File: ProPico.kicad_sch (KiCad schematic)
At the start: 16 parts

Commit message: started layout
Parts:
- removed U?: RP2040, QFN40P700X700X90-57N, symbol RP2040:RP2040
- removed U?: AMS1117-3.3, Package_TO_SOT_SMD:SOT-223-3_TabPin2, symbol Regulator_Linear:AMS1117-3.3
- added C1, C2: 18p, Capacitor_SMD:C_0402_1005Metric, symbol Device:C
- added C10, C12, C13, C14, C15, C16, C17, C7, C8: 100n, Capacitor_SMD:C_0402_1005Metric, symbol Device:C
- added C11, C9: 1u, Capacitor_SMD:C_0402_1005Metric, symbol Device:C
- added C2: 100n, Capacitor_SMD:C_0402_1005Metric_Pad0.74x0.62mm_HandSolder, symbol Device:C
- added C9: 10n C0G, Capacitor_SMD:C_0603_1608Metric_Pad1.08x0.95mm_HandSolder, symbol Device:C
- added D2, D3: LED, LED_SMD:LED_0603_1608Metric_Pad1.05x0.95mm_HandSolder, symbol Device:LED
- added J2: SWD, connector:Pico_4pin, symbol Connector_Generic:Conn_01x04
- added J3: LEFT, connector:Pico_20pin, symbol Connector_Generic:Conn_01x20
- added J4: RIGHT, connector:Pico_20pin, symbol Connector_Generic:Conn_01x20
- added JP1: EEPROM_WP, Jumper:SolderJumper-3_P2.0mm_Open_TrianglePad1.0x1.5mm, symbol Jumper:SolderJumper_3_Open
- added JP2: VREF, Jumper:SolderJumper-2_P1.3mm_Open_TrianglePad1.0x1.5mm, symbol Jumper:Jumper_2_Bridged
- added R3 (x3): 1k, Resistor_SMD:R_0402_1005Metric, symbol Device:R
- added R3 (x2): 4.7k, Resistor_SMD:R_0402_1005Metric, symbol Device:R
- added R4, R5: 27, Resistor_SMD:R_0402_1005Metric, symbol Device:R
- added R6: 5R, Resistor_SMD:R_0805_2012Metric_Pad1.20x1.40mm_HandSolder, symbol Device:R
- added R7: 150, Resistor_SMD:R_0603_1608Metric_Pad0.98x0.95mm_HandSolder, symbol Device:R
- added SW2: RES, Button_Switch_SMD:SW_SPST_B3U-1000P, symbol Switch:SW_Push
- added TP1: GND, TestPoint:TestPoint_Pad_1.5x1.5mm, symbol Connector:TestPoint
- added TP2: D-, TestPoint:TestPoint_Pad_1.5x1.5mm, symbol Connector:TestPoint
- added TP3: D+, TestPoint:TestPoint_Pad_1.5x1.5mm, symbol Connector:TestPoint
- added TP4: GP24, TestPoint:TestPoint_Pad_1.5x1.5mm, symbol Connector:TestPoint
- added TP5: GP25, TestPoint:TestPoint_Pad_1.5x1.5mm, symbol Connector:TestPoint
- added TP6: BOOTSEL, TestPoint:TestPoint_Pad_1.5x1.5mm, symbol Connector:TestPoint
- added TP7: VREG, TestPoint:TestPoint_Pad_1.5x1.5mm, symbol Connector:TestPoint
- added U1: FM24CL16B, Package_SO:SOIC-8_3.9x4.9mm_P1.27mm, symbol Memory_NVRAM:FM24CL16B
- added U3: TLV1117-33, Package_TO_SOT_SMD:SOT-223-3_TabPin2, symbol Regulator_Linear:TLV1117-33
- added U4: LM4040DBZ-3, Package_TO_SOT_SMD:SOT-23, symbol Reference_Voltage:LM4040DBZ-3
- added U5: RP2040, RP2040:RP2040-QFN-56, symbol MCU_RaspberryPi_RP2040:RP2040
- added Y1: ECS-120-12-36-AGN-TR3, Crystal:Crystal_SMD_2520-4Pin_2.5x2.0mm, symbol Device:Crystal_GND24
- C1, C5, C6: renamed from C?; footprint (none) -> Capacitor_SMD:C_0603_1608Metric_Pad1.08x0.95mm_HandSolder
- C7: renamed from C?; footprint (none) -> Capacitor_SMD:C_0402_1005Metric_Pad0.74x0.62mm_HandSolder
- C8: renamed from C?; footprint (none) -> Capacitor_SMD:C_0805_2012Metric_Pad1.18x1.45mm_HandSolder
- D1: renamed from D?; value 500mA -> B5819W; footprint (none) -> Diode_SMD:D_SOD-123
- FB1: renamed from FB?; footprint (none) -> Inductor_SMD:L_0805_2012Metric_Pad1.15x1.40mm_HandSolder
- J1: renamed from J?; footprint (none) -> Connector_USB:USB_C_Receptacle_Palconn_UTC16-G
- R1: renamed from R?; value 10k -> 1k; footprint (none) -> Resistor_SMD:R_0402_1005Metric_Pad0.72x0.64mm_HandSolder
- R2: renamed from NO_FIT; footprint (none) -> Resistor_SMD:R_0402_1005Metric_Pad0.72x0.64mm_HandSolder; now not fitted
- R3, R4: renamed from R?; footprint (none) -> Resistor_SMD:R_0402_1005Metric_Pad0.72x0.64mm_HandSolder
- SW1: renamed from SW?; value TS-1092S-B3D2-G -> BOOTSEL; footprint (none) -> Button_Switch_SMD:SW_SPST_B3U-1000P
- U2: renamed from U?; footprint Package_SO:SOIC-8_5.23x5.23mm_P1.27mm -> W25Q16JVUXIQ_TR:IC_W25Q16JVUXIQ_TR
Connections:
- net +3V3: now also C10.1, C11.1, C12.1, C13.1, C14.1, C15.1, C16.1, C17.1, C2.1, J4.16 (Pin_16), JP1.1 (A), R3.1, R3.1, R6.2, R7.2, U1.8 (VDD), U3.2 (VO), U5.1 (IOVDD), U5.10 (IOVDD), U5.22 (IOVDD), U5.33 (IOVDD), U5.42 (IOVDD), U5.44 (VREG_IN), U5.48 (USB_VDD), U5.49 (IOVDD); no longer C8.1
- net +5V: now also J4.19 (Pin_19), U3.3 (VI)
- net D+: now also R4.1, TP3.1
- net D-: now also R5.1, TP2.1
- net GND: now also C1.2, C10.2, C11.2, C12.2, C13.2, C14.2, C15.2, C16.2, C17.2, C2.2, C2.2, C7.2, C8.2, C9.2, C9.2, J2.2 (Pin_2), J3.13 (Pin_13), J3.18 (Pin_18), J3.3 (Pin_3), J3.8 (Pin_8), J4.13 (Pin_13), J4.18 (Pin_18), J4.3 (Pin_3), J4.8 (Pin_8), JP1.3 (B), R3.2, R3.2, SW2.2, TP1.1, U1.4 (VSS), U3.1 (GND), U4.2 (A), U5.19 (TESTEN), U5.57 (GND), Y1.2, Y1.4
- net QSPI_SCLK: now also U5.52 (QSPI_SCLK)
- net QSPI_SD0: now also U5.53 (QSPI_SD0)
- net QSPI_SD1: now also U5.55 (QSPI_SD1)
- net QSPI_SD2: now also U5.54 (QSPI_SD2)
- net QSPI_SD3: now also U5.51 (QSPI_SD3)
- net QSPI_SS: now also U5.56 (QSPI_SS)
- net VBUS: now also D1.2 (A), J1.A4 (VBUS), J1.A9 (VBUS), J1.B4 (VBUS), J1.B9 (VBUS), J4.20 (Pin_20); no longer C1.1, D1.1 (K), FB1.1
- net at R1.2, SW1.2: now also TP6.1
- new net: C8.1, R6.1
- new net: D2.1 (K), R3.1
- new net: C2.1, R3.2, Y1.1
- new net: R5.2, U5.46 (USB_DM)
- new net: R4.2, U5.47 (USB_DP)
- new net: D3.1 (K), R3.1
- new net +1V1: C7.1, C8.1, C9.1, TP7.1, U5.23 (DVDD), U5.45 (VREG_VOUT), U5.50 (DVDD)
- new net +5VD: C1.1, D1.1 (K), FB1.1
- new net 3V0_VREF: JP2.2 (B), R7.1, U4.1 (K)
- new net ADC_AVDD: C9.1, J4.15 (Pin_15), JP2.1 (A), U5.43 (ADC_AVDD)
- new net EEPROM_SCL: D3.2 (A), R3.2, TP5.1, U1.6 (SCL), U5.37 (GPIO25)
- new net EEPROM_SDA: R3.2, TP4.1, U1.5 (SDA), U5.36 (GPIO24)
- new net EEPROM_WP: JP1.2 (C), U1.7 (WP)
- new net GPIO0: J3.1 (Pin_1), U5.2 (GPIO0)
- new net GPIO1: J3.2 (Pin_2), U5.3 (GPIO1)
- new net GPIO10: J3.14 (Pin_14), U5.13 (GPIO10)
- new net GPIO11: J3.15 (Pin_15), U5.14 (GPIO11)
- new net GPIO12: J3.16 (Pin_16), U5.15 (GPIO12)
- new net GPIO13: J3.17 (Pin_17), U5.16 (GPIO13)
- new net GPIO14: J3.19 (Pin_19), U5.17 (GPIO14)
- new net GPIO15: J3.20 (Pin_20), U5.18 (GPIO15)
- new net GPIO16: J4.1 (Pin_1), U5.27 (GPIO16)
- new net GPIO17: J4.2 (Pin_2), U5.28 (GPIO17)
- new net GPIO18: J4.4 (Pin_4), U5.29 (GPIO18)
- new net GPIO19: J4.5 (Pin_5), U5.30 (GPIO19)
- new net GPIO2: J3.4 (Pin_4), U5.4 (GPIO2)
- new net GPIO20: J4.6 (Pin_6), U5.31 (GPIO20)
- new net GPIO21: J4.7 (Pin_7), U5.32 (GPIO21)
- new net GPIO22: J4.9 (Pin_9), U5.34 (GPIO22)
- new net GPIO23: D2.2 (A), U5.35 (GPIO23)
- new net GPIO26_ADC0: J4.11 (Pin_11), U5.38 (GPIO26_ADC0)
- new net GPIO27_ADC1: J4.12 (Pin_12), U5.39 (GPIO27_ADC1)
- new net GPIO28_ADC2: J4.14 (Pin_14), U5.40 (GPIO28_ADC2)
- new net GPIO29_ADC3: J4.17 (Pin_17), U5.41 (GPIO29_ADC3)
- new net GPIO3: J3.5 (Pin_5), U5.5 (GPIO3)
- new net GPIO4: J3.6 (Pin_6), U5.6 (GPIO4)
- new net GPIO5: J3.7 (Pin_7), U5.7 (GPIO5)
- new net GPIO6: J3.9 (Pin_9), U5.8 (GPIO6)
- new net GPIO7: J3.10 (Pin_10), U5.9 (GPIO7)
- new net GPIO8: J3.11 (Pin_11), U5.11 (GPIO8)
- new net GPIO9: J3.12 (Pin_12), U5.12 (GPIO9)
- new net RUN: J2.4 (Pin_4), J4.10 (Pin_10), SW2.1, U5.26 (RUN)
- new net SWCLK: J2.1 (Pin_1), U5.24 (SWCLK)
- new net SWD: J2.3 (Pin_3), U5.25 (SWD)
- new net XIN: C1.1, U5.20 (XIN), Y1.3
- new net XOUT: R3.1, U5.21 (XOUT)
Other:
- note added: "B3U-1000P"
- note added: "Make sure C10 is close to pin 44 of RP2040"
- note added: "Make sure C8 is close to pin 45 of RP2040"
- note added: "or 24C04"
- note removed: "BOOTSEL"
- moved on the sheet: C1, C5, C6, C7, C8, D1, FB1, J1, R1, R3, R4, SW1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

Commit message: started layout
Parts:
- removed C5, C6: 2.2u, Capacitor_SMD:C_0603_1608Metric_Pad1.08x0.95mm_HandSolder, symbol Device:C
- removed FB1: 100 @ 100MHz, Inductor_SMD:L_0805_2012Metric_Pad1.15x1.40mm_HandSolder, symbol Device:FerriteBead
- renumbered C2 to C1, C1 to C4, C7 to C5, C8 to C6, C9 to C7, TP6 to TP1, TP7 to TP2, TP5 to TP3, TP1 to TP4, TP3 to TP5, TP4 to TP6, TP2 to TP7
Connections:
- net +5VD is gone; now on net +5V: C4.1, D1.1 (K)
- net GND: now also J1.S1 (SHIELD)
- no-connect marks 3 -> 2
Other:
- note added: "AMS1117 also works"
- note added: "Make sure C10 is close to pin 45 of RP2040"
- note added: "Make sure C12 is close to pin 44 of RP2040"
- note removed: "Make sure C10 is close to pin 44 of RP2040"
- note removed: "Make sure C8 is close to pin 45 of RP2040"
- moved on the sheet: C4, C5

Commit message: progress on layout
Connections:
- net DN: now reaches R5.2, U5.46 (USB_DM)
- net DP: now reaches R4.2, U5.47 (USB_DP)
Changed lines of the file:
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@@
     (effects (font (size 1.27 1.27)) (justify right bottom))
+  )
+  (label "DN" (at 286.385 90.805 0) (fields_autoplaced)
+    (effects (font (size 1.27 1.27)) (justify left bottom))
+    (property "Netclass" "diif_usb" (at 286.385 92.075 0)
+      (effects (font (size 1.27 1.27) italic) (justify left) hide)
+    )
   )
   (label "GPIO21" (at 297.18 151.765 180) (fields_autoplaced)
@@
   (label "D+" (at 52.705 52.07 180) (fields_autoplaced)
     (effects (font (size 1.27 1.27)) (justify right bottom))
+    (property "Netclass" "diif_usb" (at 52.705 53.34 0)
+      (effects (font (size 1.27 1.27) italic) (justify right) hide)
+    )
   )
   (label "EEPROM_SCL" (at 348.615 113.665 270) (fields_autoplaced)
@@
     (effects (font (size 1.27 1.27)) (justify left bottom))
   )
+  (label "DP" (at 286.385 88.265 0) (fields_autoplaced)
+    (effects (font (size 1.27 1.27)) (justify left bottom))
+    (property "Netclass" "diif_usb" (at 286.385 89.535 0)
+      (effects (font (size 1.27 1.27) italic) (justify left) hide)
+    )
+  )
   (label "D-" (at 52.705 46.99 180) (fields_autoplaced)
     (effects (font (size 1.27 1.27)) (justify right bottom))
+    (property "Netclass" "diif_usb" (at 52.705 48.26 0)
+      (effects (font (size 1.27 1.27) italic) (justify right) hide)
+    )
   )
   (label "GPIO10" (at 297.18 123.825 180) (fields_autoplaced)

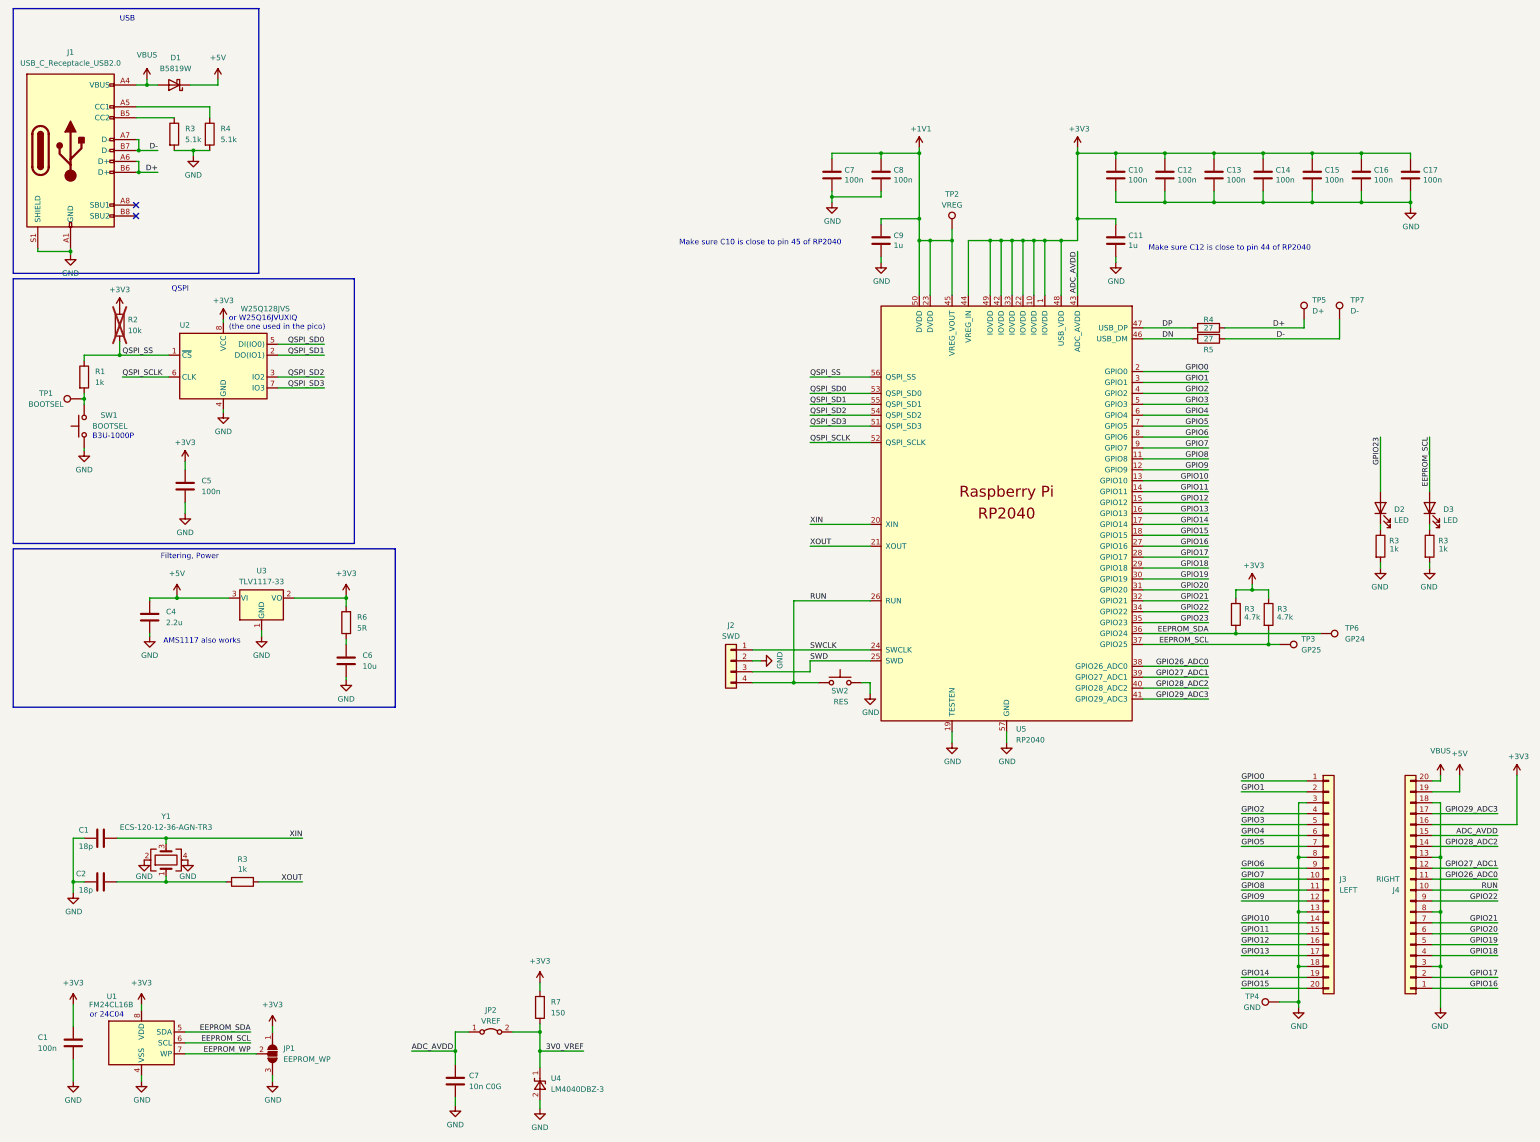
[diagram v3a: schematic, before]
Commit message: finished silkscreen
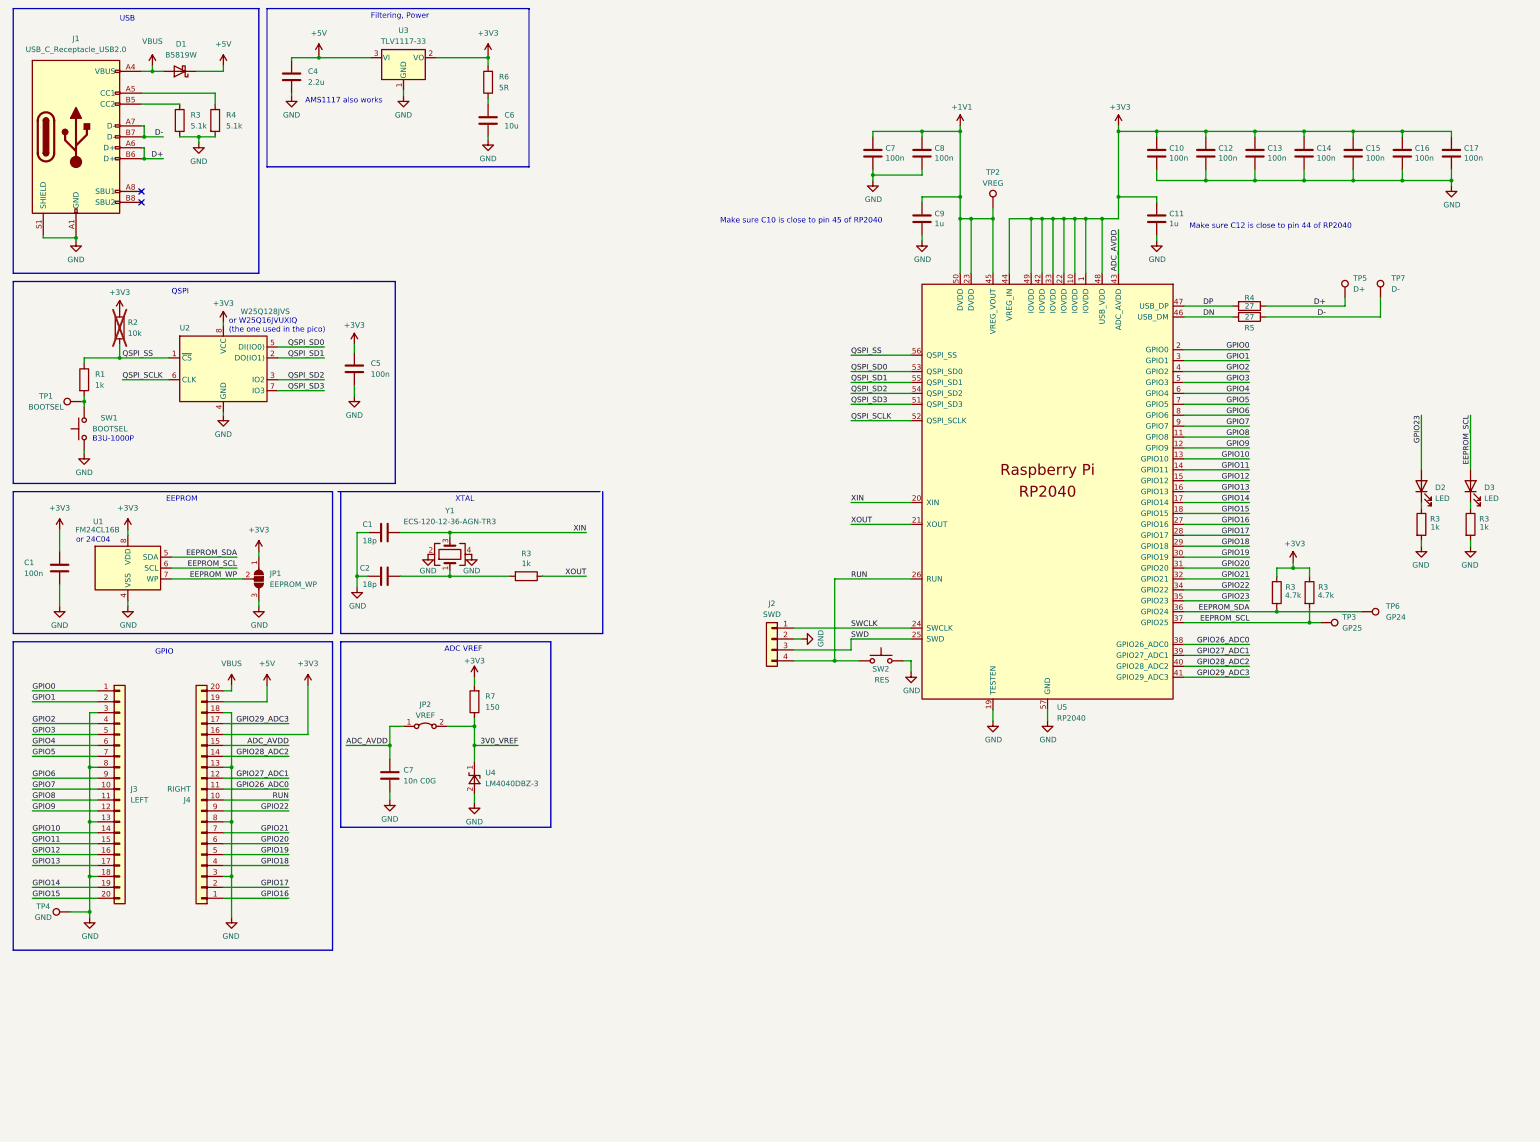
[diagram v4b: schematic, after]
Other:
- note added: "ADC VREF"
- note added: "EEPROM"
- note added: "GPIO"
- note added: "XTAL"
- moved on the sheet: C1, C10, C11, C12, C13, C14, C15, C16, C17, C2, C4, C5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

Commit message: updated schematic
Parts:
- R6: value 5R -> 1R
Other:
- note added: "when using TLV761 replace with jumper"
- note removed: "AMS1117 also works"
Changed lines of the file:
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@@
+    (stroke (width 0) (type default))
+  )
+  (polyline (pts (xy 96.52 45.72) (xy 115.57 45.72))
     (stroke (width 0) (type default))
   )
@@
     (stroke (width 0) (type default))
   )
+  (polyline (pts (xy 115.57 45.72) (xy 127.635 33.655))
+    (stroke (width 0) (type default))
+  )
   (wire (pts (xy 35.56 95.25) (xy 35.56 96.52))
     (stroke (width 0) (type default))
@@
     (stroke (width 0) (type default))
   )
+  (polyline (pts (xy 125.73 33.655) (xy 127.635 33.655))
+    (stroke (width 0) (type default))
+  )
   (wire (pts (xy 272.415 75.565) (xy 272.415 62.865))
     (stroke (width 0) (type default))
@@
     (stroke (width 0) (type default))
   )
+  (polyline (pts (xy 127.635 33.655) (xy 127.635 35.56))
+    (stroke (width 0) (type default))
+  )
   (wire (pts (xy 38.735 208.28) (xy 23.495 208.28))
     (stroke (width 0) (type default))
@@
     (effects (font (size 1.27 1.27)) (justify left bottom))
   )
-  (text "AMS1117 also works" (at 86.995 36.195 0)
+  (text "when using TLV761\nreplace with jumper" (at 96.52 45.085 0)
     (effects (font (size 1.27 1.27)) (justify left bottom))
   )
@@
       (effects (font (size 1.27 1.27)) (justify right))
     )
-    (property "Value" "5R" (at 132.08 32.385 0)
+    (property "Value" "1R" (at 132.08 32.385 0)
       (effects (font (size 1.27 1.27)) (justify right))
     )

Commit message: wip adding part numbers to components
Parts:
- C1, C10, C12, C13, C14, C15, C16, C17, C5, C7, C8: LCSC (none) -> C77020; P/N (none) -> GRM155R71H104KE14D
- C4: LCSC (none) -> C57895; P/N (none) -> CL10A225KA8NNNC
- C6: LCSC (none) -> C162422; P/N (none) -> GRM21BR6YA106KE43L
- D1: LCSC (none) -> C552930; P/N (none) -> PMEG6010CEGWJ
- J1: LCSC (none) -> C165948; P/N (none) -> TYPE-C-31-M-12
- R2: value 10k -> DNP
- R3, R4: LCSC (none) -> C105873; P/N (none) -> RC0402JR-075K1
- R6: value 1R -> 470mOhm; LCSC (none) -> C2930220; P/N (none) -> FRL0805FR470TS
- SW1, SW2: LCSC (none) -> C231329; P/N (none) -> B3U-1000P
- U1: LCSC (none) -> C31082; P/N (none) -> FM24CL16B
- U2: value W25Q128JVS -> W25Q16JVUXIQ; LCSC (none) -> C2843335; P/N (none) -> W25Q16JVUXIQ
- U3: value TLV1117-33 -> AMS1117-3.3; LCSC (none) -> C347222; P/N (none) -> AMS1117-3.3
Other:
- note added: "10k"
- note added: "Compatible examples: FM24CL16B - fram (C31082) 24C04 - eeprom (C118280) 24C16 - larger eeprom (C79946) etc..."
- note added: "larger ones require a different footprint"
- note added: "when using MLCC stable LDO replace with jumper"
- note removed: "B3U-1000P"
- note removed: "or 24C04"
- note removed: "or W25Q16JVUXIQ (the one used in the pico)"
- note removed: "when using TLV761 replace with jumper"
- moved on the sheet: C1, C5, JP1, U1
